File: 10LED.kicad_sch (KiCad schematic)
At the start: 20 parts

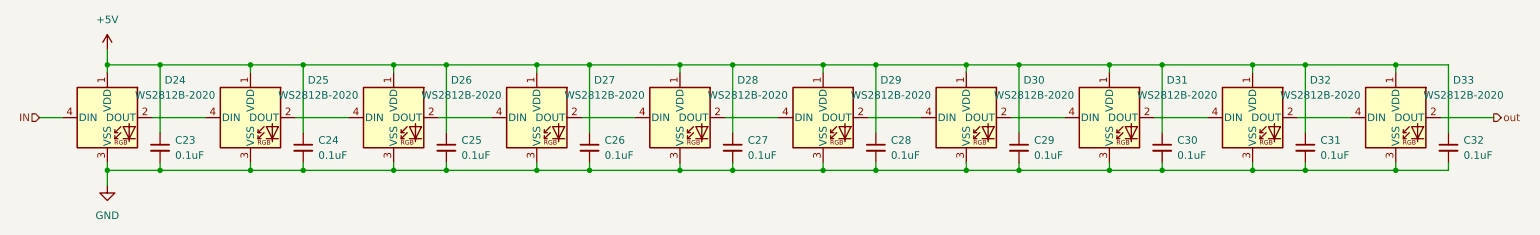
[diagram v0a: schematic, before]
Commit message: 外周LEDを116個に修正
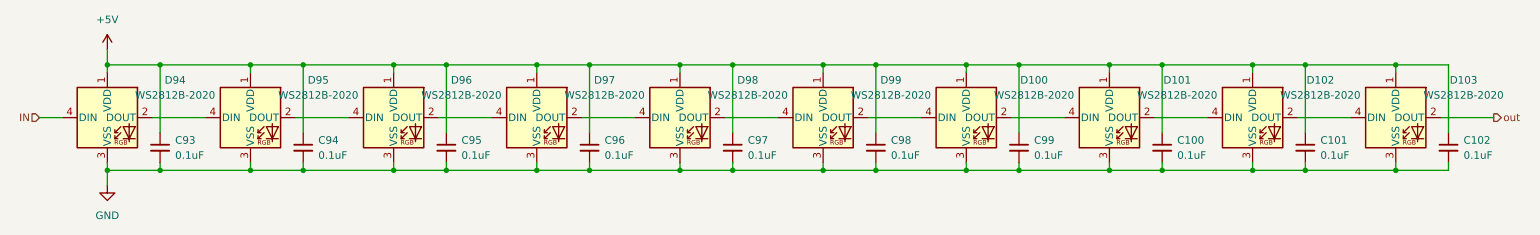
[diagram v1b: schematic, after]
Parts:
- renumbered C30 to C100, C31 to C101, C32 to C102, C23 to C93, C24 to C94, C25 to C95, C26 to C96, C27 to C97, C28 to C98, C29 to C99, D30 to D100, D31 to D101, D32 to D102, D33 to D103, D24 to D94, D25 to D95, D26 to D96, D27 to D97, D28 to D98, D29 to D99
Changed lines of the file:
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@@
 		(dnp no)
 		(fields_autoplaced yes)
-		(property "Reference" "D28"
+		(property "Reference" "D98"
 			(at 146.05 90.2014 0)
 			(effects
@@
 		(dnp no)
 		(fields_autoplaced yes)
-		(property "Reference" "D31"
+		(property "Reference" "D101"
 			(at 218.44 90.2014 0)
 			(effects
@@
 		(dnp no)
 		(fields_autoplaced yes)
-		(property "Reference" "#PWR015"
+		(property "Reference" "#PWR029"
 			(at 38.1 88.9 0)
 			(effects
@@
 		(dnp no)
 		(fields_autoplaced yes)
-		(property "Reference" "C28"
+		(property "Reference" "C98"
 			(at 170.18 100.3362 0)
 			(effects
@@
 		(dnp no)
 		(fields_autoplaced yes)
-		(property "Reference" "D24"
+		(property "Reference" "D94"
 			(at 49.53 90.2014 0)
 			(effects
@@
 		(dnp no)
 		(fields_autoplaced yes)
-		(property "Reference" "C30"
+		(property "Reference" "C100"
 			(at 218.44 100.3362 0)
 			(effects
@@
 		(dnp no)
 		(fields_autoplaced yes)
-		(property "Reference" "D32"
+		(property "Reference" "D102"
 			(at 242.57 90.2014 0)
 			(effects
@@
 		(dnp no)
 		(fields_autoplaced yes)
-		(property "Reference" "C27"
+		(property "Reference" "C97"
 			(at 146.05 100.3362 0)
 			(effects
@@
 		(dnp no)
 		(fields_autoplaced yes)
-		(property "Reference" "C31"
+		(property "Reference" "C101"
 			(at 242.57 100.3362 0)
 			(effects
@@
 		(dnp no)
 		(fields_autoplaced yes)
-		(property "Reference" "C23"
+		(property "Reference" "C93"
 			(at 49.53 100.3362 0)
 			(effects
@@
 		(dnp no)
 		(fields_autoplaced yes)
-		(property "Reference" "C26"
+		(property "Reference" "C96"
 			(at 121.92 100.3362 0)
 			(effects
@@
 		(dnp no)
 		(fields_autoplaced yes)
-		(property "Reference" "D26"
+		(property "Reference" "D96"
 			(at 97.79 90.2014 0)
 			(effects
@@
 		(dnp no)
 		(fields_autoplaced yes)
-		(property "Reference" "D33"
+		(property "Reference" "D103"
 			(at 266.7 90.2014 0)
 			(effects
@@
 		(dnp no)
 		(fields_autoplaced yes)
-		(property "Reference" "D30"
+		(property "Reference" "D100"
 			(at 194.31 90.2014 0)
 			(effects
@@
 		(dnp no)
 		(fields_autoplaced yes)
-		(property "Reference" "C29"
+		(property "Reference" "C99"
 			(at 194.31 100.3362 0)
 			(effects
@@
 		(dnp no)
 		(fields_autoplaced yes)
-		(property "Reference" "D25"
+		(property "Reference" "D95"
 			(at 73.66 90.2014 0)
 			(effects
@@
 		(dnp no)
 		(fields_autoplaced yes)
-		(property "Reference" "D27"
+		(property "Reference" "D97"
 			(at 121.92 90.2014 0)
 			(effects
@@
 		(dnp no)
 		(fields_autoplaced yes)
-		(property "Reference" "#PWR016"
+		(property "Reference" "#PWR030"
 			(at 38.1 114.3 0)
 			(effects
@@
 		(dnp no)
 		(fields_autoplaced yes)
-		(property "Reference" "D29"
+		(property "Reference" "D99"
 			(at 170.18 90.2014 0)
 			(effects
@@
 		(dnp no)
 		(fields_autoplaced yes)
-		(property "Reference" "C24"
+		(property "Reference" "C94"
 			(at 73.66 100.3362 0)
 			(effects
@@
 		(dnp no)
 		(fields_autoplaced yes)
-		(property "Reference" "C25"
+		(property "Reference" "C95"
 			(at 97.79 100.3362 0)
 			(effects
@@
 		(dnp no)
 		(fields_autoplaced yes)
-		(property "Reference" "C32"
+		(property "Reference" "C102"
 			(at 266.7 100.3362 0)
 			(effects

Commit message: 部品修正
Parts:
- D100, D101, D102, D103, D94, D95, D96, D97, D98, D99: footprint LED_SMD:LED_WS2812B_PLCC4_5.0x5.0mm_P3.2mm -> LED_SMD:LED_WS2812B-2020_PLCC4_2.0x2.0mm; symbol LED:WS2812B -> LED:WS2812B-2020
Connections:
- net +5V: now also D100.4 (VDD), D101.4 (VDD), D102.4 (VDD), D103.4 (VDD), D94.4 (VDD), D95.4 (VDD), D96.4 (VDD), D97.4 (VDD), D98.4 (VDD), D99.4 (VDD); no longer D100.1 (VDD), D101.1 (VDD), D102.1 (VDD), D103.1 (VDD), D94.1 (VDD), D95.1 (VDD), D96.1 (VDD), D97.1 (VDD), D98.1 (VDD), D99.1 (VDD)
- net GND: now also D100.2 (VSS), D101.2 (VSS), D102.2 (VSS), D103.2 (VSS), D94.2 (VSS), D95.2 (VSS), D96.2 (VSS), D97.2 (VSS), D98.2 (VSS), D99.2 (VSS); no longer D100.3 (VSS), D101.3 (VSS), D102.3 (VSS), D103.3 (VSS), D94.3 (VSS), D95.3 (VSS), D96.3 (VSS), D97.3 (VSS), D98.3 (VSS), D99.3 (VSS)
- net IN: now also D94.3 (DIN); no longer D94.4 (DIN)
- net out: now also D103.1 (DOUT); no longer D103.2 (DOUT)
- new net: D98.1 (DOUT), D99.3 (DIN)
- new net: D97.1 (DOUT), D98.3 (DIN)
- new net: D101.1 (DOUT), D102.3 (DIN)
- new net: D100.1 (DOUT), D101.3 (DIN)
- new net: D94.1 (DOUT), D95.3 (DIN)
- new net: D102.1 (DOUT), D103.3 (DIN)
- new net: D96.1 (DOUT), D97.3 (DIN)
- new net: D95.1 (DOUT), D96.3 (DIN)
- new net: D100.3 (DIN), D99.1 (DOUT)
